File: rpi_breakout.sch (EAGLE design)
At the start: 26 parts, among them U2 TXB0108, U3 TXB0108

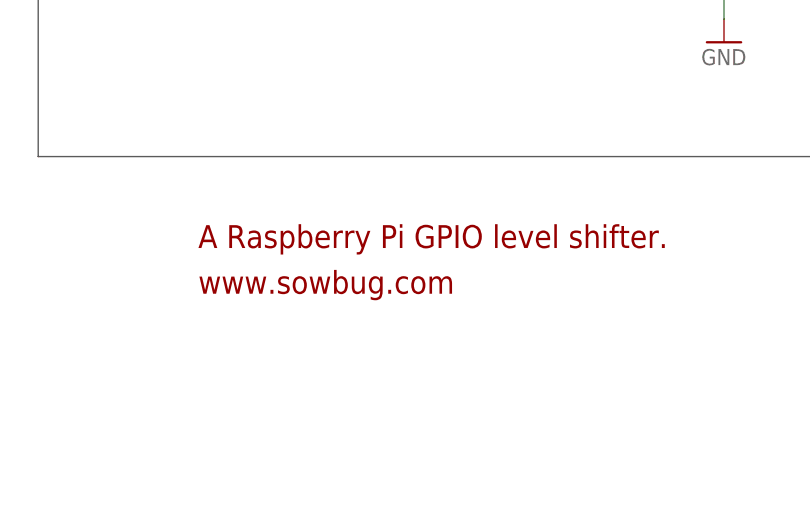
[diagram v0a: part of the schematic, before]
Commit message: Fix schematic URL. Board PNG with pour.
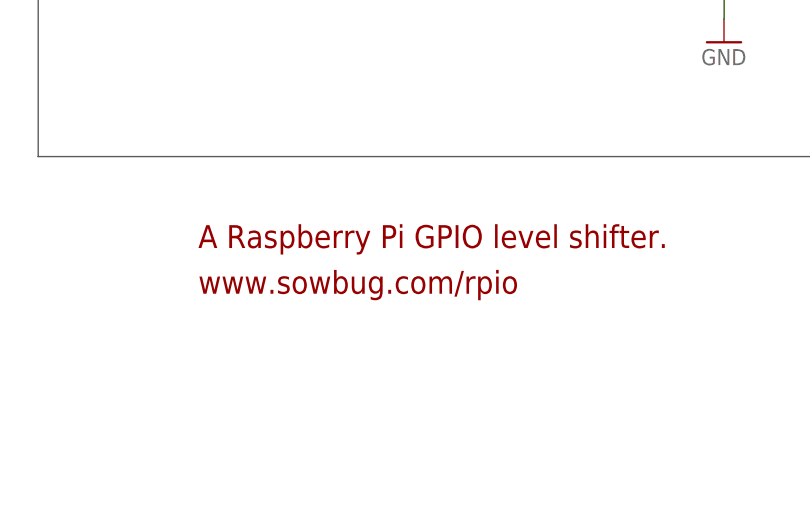
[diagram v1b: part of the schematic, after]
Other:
- note added: "www.sowbug.com/rpio"
- note removed: "www.sowbug.com"
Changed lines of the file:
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@@
 <text x="134.62" y="175.26" size="5.08" layer="97" font="vector">Level Translation</text>
 <text x="149.86" y="30.48" size="2.54" layer="94" font="vector">A Raspberry Pi GPIO level shifter.</text>
-<text x="149.86" y="25.4" size="2.54" layer="94" font="vector">www.sowbug.com</text>
+<text x="149.86" y="25.4" size="2.54" layer="94" font="vector">www.sowbug.com/rpio</text>
 </plain>
 <instances>

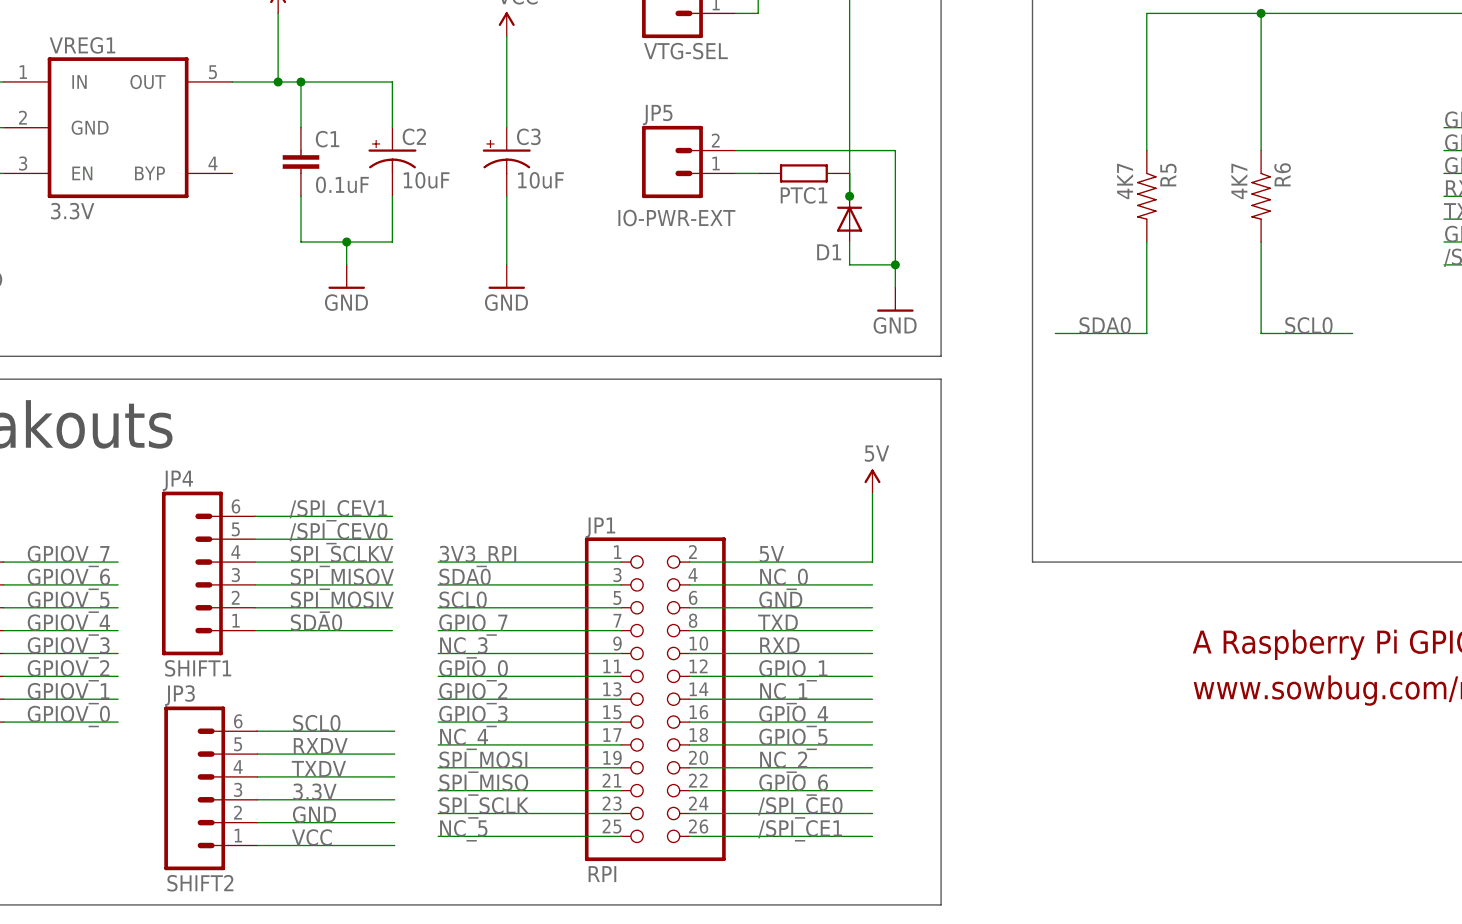
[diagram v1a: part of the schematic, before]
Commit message: Added through-hole pull-up resistors.  Rounded corners.  Larger labels.
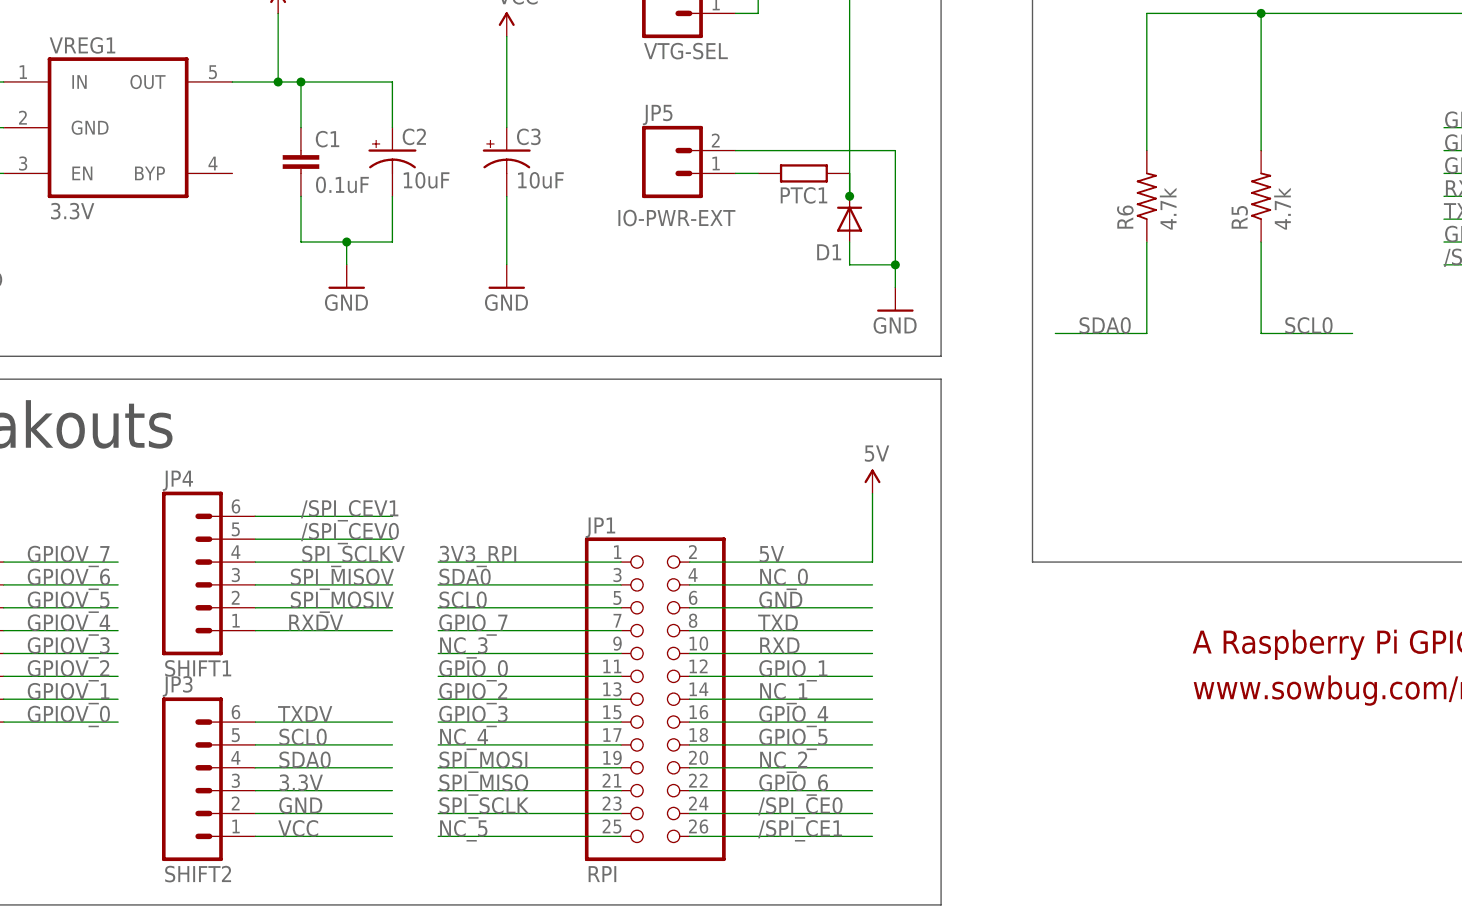
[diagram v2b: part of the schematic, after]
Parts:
- R5, R6: value 4K7 -> 4.7k; device SparkFun:RESISTOR0805-RES -> rcl:R-US_0207/10
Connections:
- net 3V3_RPI: now also R5.2, R6.2; no longer R5.1, R6.1
- net RXDV: now also JP4.1; no longer JP3.5
- net SCL0: now also JP3.5, R5.1; no longer JP3.6, R6.2
- net SDA0: now also JP3.4, R6.1; no longer JP4.1, R5.2
- net TXDV: now also JP3.6; no longer JP3.4
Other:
- moved on the sheet: JP3, R5, R6

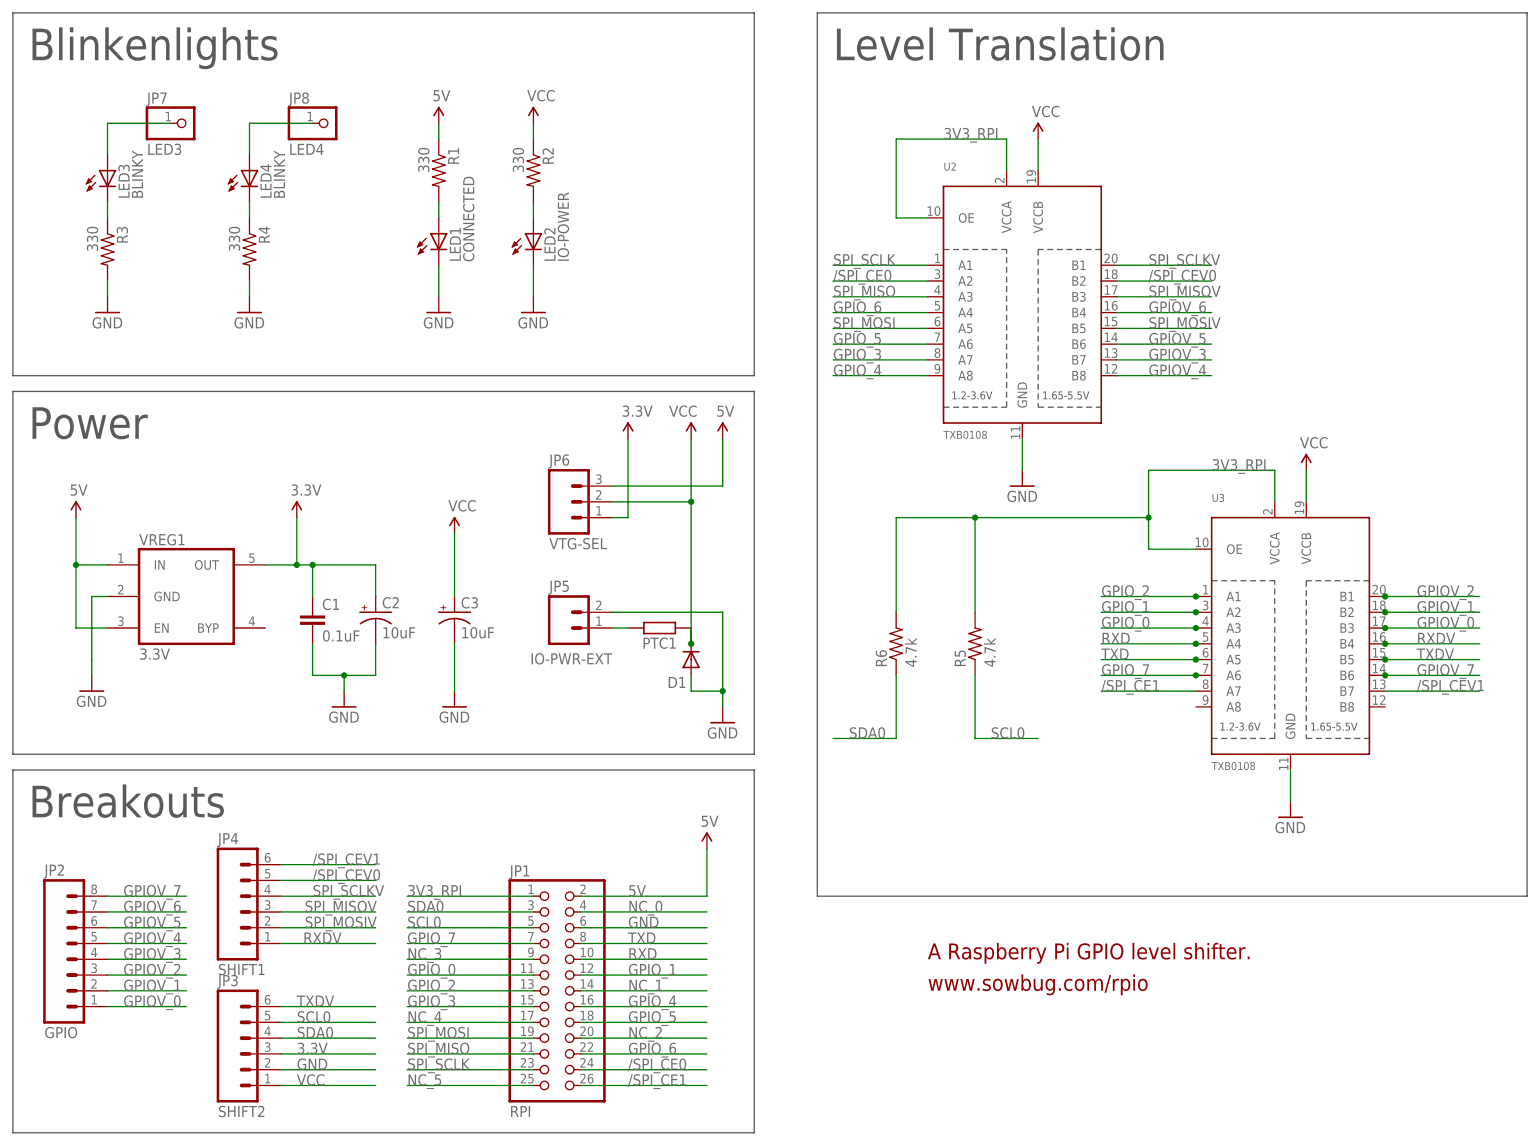
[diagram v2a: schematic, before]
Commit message: Relaxed and shrank layout a bit.  Added a blinkenlight.
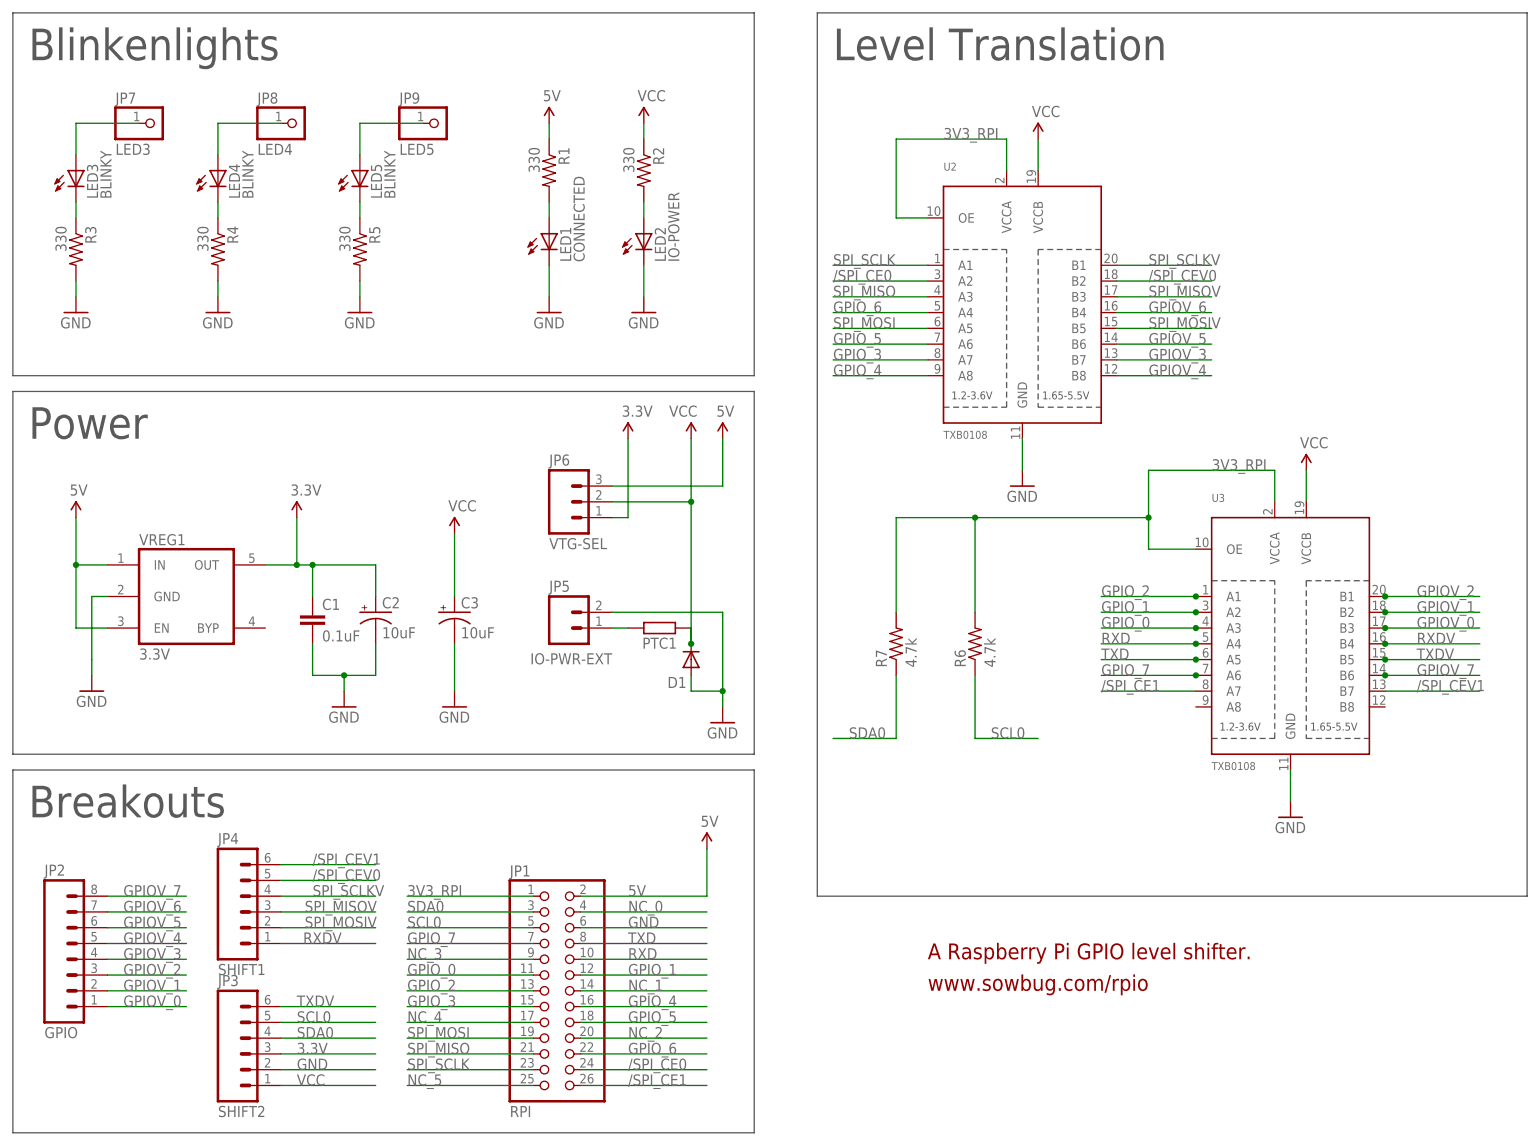
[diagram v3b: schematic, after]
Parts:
- added JP9: LED5, adafruit:PINHD-1X1CB
- added LED5: BLINKY, adafruit:LEDCHIPLED_0805
- added R7: 4.7k, rcl:R-US_0207/10
- R5: value 4.7k -> 330; device rcl:R-US_0207/10 -> SparkFun:RESISTOR0805-RES
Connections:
- new net LED5_JP1: JP9.1, LED5.A
- new net N$5: LED5.C, R5.1
- net 3V3_RPI: now also R7.2; no longer R5.2
- net GND: now also R5.2
- net SCL0: now also R6.1; no longer R5.1
- net SDA0: now also R7.1; no longer R6.1
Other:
- moved on the sheet: JP7, JP8, LED1, LED2, LED3, LED4, R1, R2, R3, R4, R5, R6

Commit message: Interim checkin. Autorouter is SLOW today.
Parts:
- added Q1, Q2: BSS138, rpi_breakout:SPARKFUN_MOSFET-NCHANNELSMD
- C1: device SparkFun:CAP0805 -> rpi_breakout:SPARKFUN_CAP0805
- C2, C3: device SparkFun:CAP_POL1206 -> rpi_breakout:SPARKFUN_CAP_POL1206
- D1: device SparkFun-DiscreteSemi:DIODESOD -> rpi_breakout:SPARKFUN-DISCRETESEMI_DIODESOD
- JP1: device pinhead:PINHD-2X13 -> rpi_breakout:PINHEAD_PINHD-2X13
- JP2: device SparkFun:M08LOCK -> rpi_breakout:SPARKFUN_M08LOCK
- JP3, JP4: device SparkFun:M06FEMALE_LOCK -> rpi_breakout:SPARKFUN_M06LOCK
- JP5: device SparkFun:M02PTH -> rpi_breakout:SPARKFUN_M02LOCK
- JP6: device SparkFun:M03PTH -> rpi_breakout:SPARKFUN_M03LOCK
- JP7, JP8, JP9: device adafruit:PINHD-1X1CB -> rpi_breakout:ADAFRUIT_PINHD-1X1
- LED1, LED2, LED3, LED4, LED5: device adafruit:LEDCHIPLED_0805 -> rpi_breakout:PROGRAMMER_SPARKFUN_LED
- PTC1: device rcl:R-EU_R1206 -> rpi_breakout:RCL_R-EU_R1206
- R1, R2, R3, R4, R5: device SparkFun:RESISTOR0805-RES -> rpi_breakout:SPARKFUN_RESISTOR0805-RES
- R6, R7: value 4.7k -> 10K; device rcl:R-US_0207/10 -> rpi_breakout:SPARKFUN_RESISTOR0805-RES
- U2, U3: device rpi_breakout:TXB0108PWR -> rpi_breakout:RPI_BREAKOUT_TXB0108PWR
- VREG1: device dp_devices:IC_VREG_5PINS-SOT-23-5 -> rpi_breakout:DP_DEVICES_IC_VREG_5PINS-SOT-23-5
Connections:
- new net SCLV0: JP3.5, Q2.D
- new net SDAV0: JP3.4, Q1.D
- net 3.3V: now also C1.2; no longer C1.1
- net 3V3_RPI: now also Q1.G, Q2.G
- net GND: now also C1.1; no longer C1.2
- net N$3: now also R4.1; no longer R3.1
- net N$4: now also R3.1; no longer R4.1
- net SCL0: now also Q2.S; no longer JP3.5
- net SDA0: now also Q1.S; no longer JP3.4
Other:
- moved on the sheet: R3, R4, R6, R7
